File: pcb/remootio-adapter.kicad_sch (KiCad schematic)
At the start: 63 parts, among them J1 AUX, J2 BATT, J3 ICSP, J4 Console, J5 SwitchIn, J6 SPM Connector, U1 remootio-3, U2 LM2940S-5.0, U3 AQV252GAX, U4 ATmega328PB-ANR, U5 ST232CDR, U6 AQV252GAX, U7 AQV252GAX, U8 AQV252GAX, Y1 CSTCE16M0V53-R0

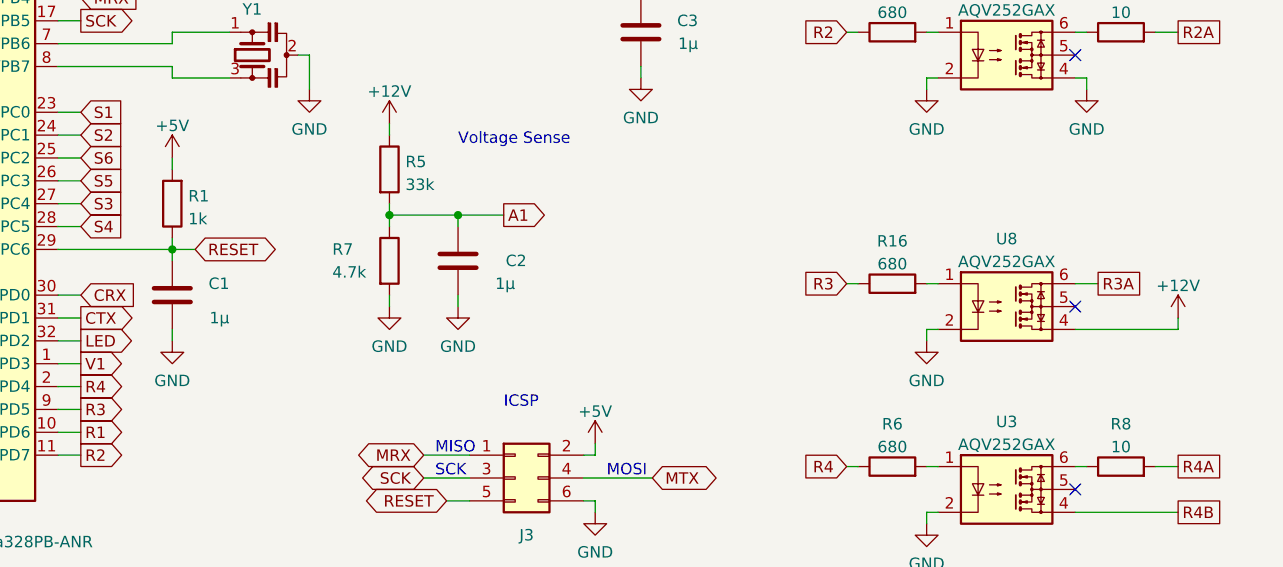
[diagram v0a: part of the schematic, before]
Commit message: Revise PCB layout for production board v1.1
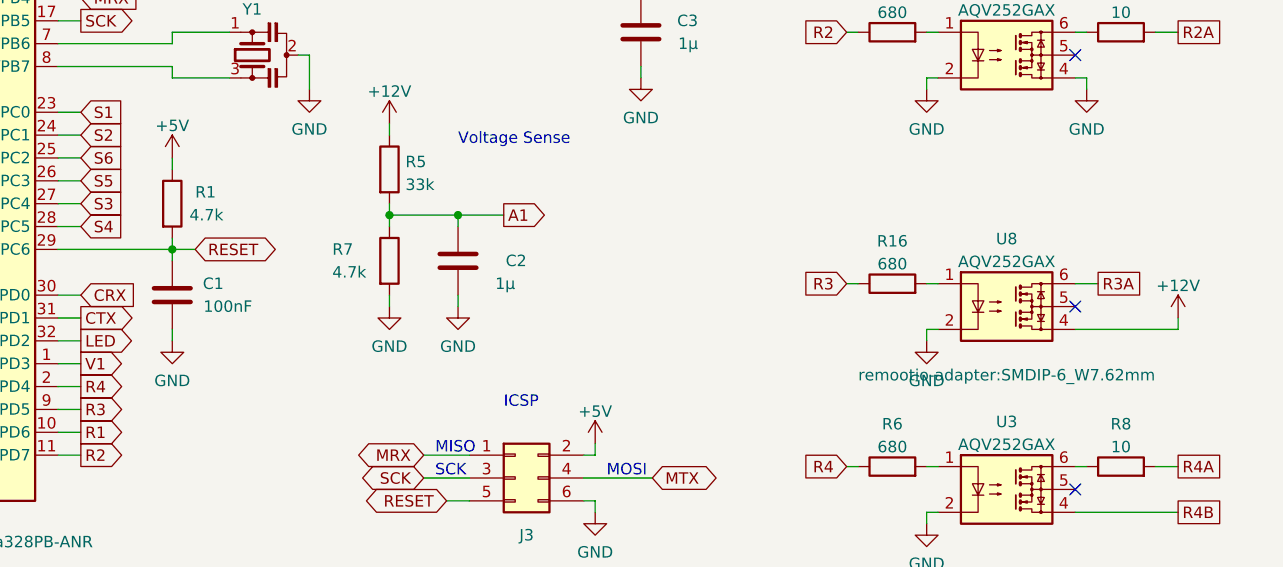
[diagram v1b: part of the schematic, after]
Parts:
- C1: value 1µ -> 100nF; LCSC C86020 -> C14663; PARTNO GRM188R71E105KA12D -> CC0603KRX7R9BB104
- R1: value 1k -> 4.7k; LCSC C21190 -> C23162; PARTNO 0603WAF1001T5E -> 0603WAF4701T5E
- U3, U6, U7, U8: footprint Package_DIP:SMDIP-6_W7.62mm -> remootio-adapter:SMDIP-6_W7.62mm
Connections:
- net +5V: now also R1.1; no longer R1.2
- net RESET: now also R1.2; no longer R1.1
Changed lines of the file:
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@@
   (title_block
     (title "Remootio Adapter - Hay Hoist")
-    (date "2024-07-22")
-    (rev "1.0")
+    (date "2024-07-30")
+    (rev "1.1")
     (company "Hyspec / 6-v")
-    (comment 1 "Ordered 5 @ JLCPCB")
   )
   (junction (at 260.35 33.02) (diameter 0) (color 0 0 0 0)
@@
   (symbol (lib_id "Device:C") (at 161.29 130.81 180) (unit 1)
     (in_bom yes) (on_board yes)
-    (property "Reference" "C1" (id 0) (at 167.64 129.54 0)
+    (property "Reference" "C1" (id 0) (at 167.005 129.54 0)
       (effects (font (size 1.27 1.27)) (justify left))
     )
-    (property "Value" "1µ" (id 1) (at 167.64 133.35 0)
+    (property "Value" "100nF" (id 1) (at 170.18 132.08 0)
       (effects (font (size 1.27 1.27)) (justify left))
     )
@@
       (effects (font (size 1.27 1.27)) hide)
     )
-    (property "Datasheet" "GRM188R71E105KA12D.pdf" (id 3) (at 161.29 130.81 0)
+    (property "Datasheet" "CC0603KRX7R9BB104.pdf" (id 3) (at 161.29 130.81 0)
       (effects (font (size 1.27 1.27)) hide)
     )
-    (property "LCSC" "C86020" (id 4) (at 161.29 130.81 90)
+    (property "LCSC" "C14663" (id 4) (at 161.29 130.81 90)
       (effects (font (size 1.27 1.27)) hide)
     )
-    (property "PARTNO" "GRM188R71E105KA12D" (id 5) (at 161.29 130.81 90)
+    (property "PARTNO" "CC0603KRX7R9BB104" (id 5) (at 161.29 130.81 90)
       (effects (font (size 1.27 1.27)) hide)
     )
@@
     (property "Reference" "U7" (id 0) (at 254 77.5802 0))
     (property "Value" "AQV252GAX" (id 1) (at 254 80.1171 0))
-    (property "Footprint" "Package_DIP:SMDIP-6_W7.62mm" (id 2) (at 254 92.71 0)
+    (property "Footprint" "remootio-adapter:SMDIP-6_W7.62mm" (id 2) (at 254 92.71 0)
       (effects (font (size 1.27 1.27)) hide)
     )
@@
     (pin "1")
   )
-  (symbol (lib_id "Device:R") (at 161.29 120.65 180) (unit 1)
-    (in_bom yes) (on_board yes) (fields_autoplaced)
-    (property "Reference" "R1" (id 0) (at 163.068 119.8153 0)
-      (effects (font (size 1.27 1.27)) (justify right))
-    )
-    (property "Value" "1k" (id 1) (at 163.068 122.3522 0)
-      (effects (font (size 1.27 1.27)) (justify right))
-    )
-    (property "Footprint" "Resistor_SMD:R_0603_1608Metric" (id 2) (at 163.068 120.65 90)
-      (effects (font (size 1.27 1.27)) hide)
-    )
-    (property "Datasheet" "0603WAF1001T5E.pdf" (id 3) (at 161.29 120.65 0)
-      (effects (font (size 1.27 1.27)) hide)
-    )
-    (property "LCSC" "C21190" (id 4) (at 161.29 120.65 90)
-      (effects (font (size 1.27 1.27)) hide)
-    )
-    (property "PARTNO" "0603WAF1001T5E" (id 5) (at 161.29 120.65 90)
-      (effects (font (size 1.27 1.27)) hide)
-    )
-    (pin "1")
-    (pin "2")
-  )
   (symbol (lib_id "Device:C") (at 97.79 144.78 270) (unit 1)
     (in_bom yes) (on_board yes)
@@
     (property "Reference" "U6" (id 0) (at 254 96.6302 0))
     (property "Value" "AQV252GAX" (id 1) (at 254 99.1671 0))
-    (property "Footprint" "Package_DIP:SMDIP-6_W7.62mm" (id 2) (at 254 111.76 0)
+    (property "Footprint" "remootio-adapter:SMDIP-6_W7.62mm" (id 2) (at 254 111.76 0)
       (effects (font (size 1.27 1.27)) hide)
     )
@@
     (pin "2")
   )
+  (symbol (lib_id "Device:R") (at 161.29 120.65 0) (unit 1)
+    (in_bom yes) (on_board yes)
+    (property "Reference" "R1" (id 0) (at 163.83 119.38 0)
+      (effects (font (size 1.27 1.27)) (justify left))
+    )
+    (property "Value" "4.7k" (id 1) (at 163.195 121.92 0)
+      (effects (font (size 1.27 1.27)) (justify left))
+    )
+    (property "Footprint" "Resistor_SMD:R_0603_1608Metric" (id 2) (at 159.512 120.65 90)
+      (effects (font (size 1.27 1.27)) hide)
+    )
+    (property "Datasheet" "0603WAF4701T5E.pdf" (id 3) (at 161.29 120.65 0)
+      (effects (font (size 1.27 1.27)) hide)
+    )
+    (property "LCSC" "C23162" (id 4) (at 161.29 120.65 90)
+      (effects (font (size 1.27 1.27)) hide)
+    )
+    (property "PARTNO" "0603WAF4701T5E" (id 5) (at 161.29 120.65 90)
+      (effects (font (size 1.27 1.27)) hide)
+    )
+    (pin "1")
+    (pin "2")
+  )
   (symbol (lib_id "power:GND") (at 193.04 132.08 0) (unit 1)
     (in_bom yes) (on_board yes) (fields_autoplaced)
@@
     (property "Reference" "U3" (id 0) (at 254 144.8902 0))
     (property "Value" "AQV252GAX" (id 1) (at 254 147.4271 0))
-    (property "Footprint" "Package_DIP:SMDIP-6_W7.62mm" (id 2) (at 254 160.02 0)
+    (property "Footprint" "remootio-adapter:SMDIP-6_W7.62mm" (id 2) (at 254 160.02 0)
       (effects (font (size 1.27 1.27)) hide)
     )
@@
     (property "Reference" "U8" (id 0) (at 254 124.5702 0))
     (property "Value" "AQV252GAX" (id 1) (at 254 127.1071 0))
-    (property "Footprint" "Package_DIP:SMDIP-6_W7.62mm" (id 2) (at 254 139.7 0)
-      (effects (font (size 1.27 1.27)) hide)
-    )
+    (property "Footprint" "remootio-adapter:SMDIP-6_W7.62mm" (id 2) (at 254 139.7 0))
     (property "Datasheet" "AQV252GAX.pdf" (id 3) (at 254 132.08 0)
       (effects (font (size 0 0)) hide)
@@
     )
     (path "/60b60661-5441-4720-a9c2-d24e0064a5a0"
-      (reference "C1") (unit 1) (value "1µ") (footprint "Capacitor_SMD:C_0603_1608Metric")
+      (reference "C1") (unit 1) (value "100nF") (footprint "Capacitor_SMD:C_0603_1608Metric")
     )
     (path "/7e705115-9ba3-4ade-9c21-0ecd8cb7d552"
@@
       (reference "J6") (unit 1) (value "SPM Connector") (footprint "TerminalBlock_Phoenix:TerminalBlock_Phoenix_MKDS-1,5-8-5.08_1x08_P5.08mm_Horizontal")
     )
-    (path "/8234446a-2afe-4a9b-9a53-39dd33467d7e"
-      (reference "R1") (unit 1) (value "1k") (footprint "Resistor_SMD:R_0603_1608Metric")
+    (path "/b6fb716c-d73d-4cb2-82ba-361713ac886b"
+      (reference "R1") (unit 1) (value "4.7k") (footprint "Resistor_SMD:R_0603_1608Metric")
     )
     (path "/5de2599c-fbeb-484b-8fcf-91d79ad8d43b"
@@
     )
     (path "/c1bc3891-d4c5-4a3d-af07-e42d28535bf4"
-      (reference "U3") (unit 1) (value "AQV252GAX") (footprint "Package_DIP:SMDIP-6_W7.62mm")
+      (reference "U3") (unit 1) (value "AQV252GAX") (footprint "remootio-adapter:SMDIP-6_W7.62mm")
     )
     (path "/ebaf2b81-8432-4142-9920-6faf4f23aa7d"
@@
     )
     (path "/a85d6911-9680-422b-a8e9-1367fbf4022a"
-      (reference "U6") (unit 1) (value "AQV252GAX") (footprint "Package_DIP:SMDIP-6_W7.62mm")
+      (reference "U6") (unit 1) (value "AQV252GAX") (footprint "remootio-adapter:SMDIP-6_W7.62mm")
     )
     (path "/7bad97ee-b0f3-485e-b963-4bac43e534c7"
-      (reference "U7") (unit 1) (value "AQV252GAX") (footprint "Package_DIP:SMDIP-6_W7.62mm")
+      (reference "U7") (unit 1) (value "AQV252GAX") (footprint "remootio-adapter:SMDIP-6_W7.62mm")
     )
     (path "/d3bed3fa-52c1-4a23-9ef9-5c53ebed779a"
-      (reference "U8") (unit 1) (value "AQV252GAX") (footprint "Package_DIP:SMDIP-6_W7.62mm")
+      (reference "U8") (unit 1) (value "AQV252GAX") (footprint "remootio-adapter:SMDIP-6_W7.62mm")
     )
     (path "/4c0707aa-6e6f-4ade-ba13-26f73eef7bfd"

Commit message: Minor cosmetic footprint adjustment
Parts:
- D1: footprint LED_THT:LED_D3.0mm_Clear -> remootio-adapter:bivar-led
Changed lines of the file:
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@@
   (title_block
     (title "Remootio Adapter - Hay Hoist")
-    (date "2024-07-30")
+    (date "2024-08-06")
     (rev "1.1")
     (company "Hyspec / 6-v")
@@
     (property "Reference" "D1" (id 0) (at 217.4875 71.6112 0))
     (property "Value" "VAOL-3GWY4" (id 1) (at 217.4875 74.1481 0))
-    (property "Footprint" "LED_THT:LED_D3.0mm_Clear" (id 2) (at 215.9 77.47 0)
+    (property "Footprint" "remootio-adapter:bivar-led" (id 2) (at 215.9 77.47 0)
       (effects (font (size 1.27 1.27)) hide)
     )
@@
     )
     (path "/edcf1849-349d-4d22-9ff8-a3b3b9d08838"
-      (reference "D1") (unit 1) (value "VAOL-3GWY4") (footprint "LED_THT:LED_D3.0mm_Clear")
+      (reference "D1") (unit 1) (value "VAOL-3GWY4") (footprint "remootio-adapter:bivar-led")
     )
     (path "/201afaf1-c2db-44e9-a493-4de777d50aa5"

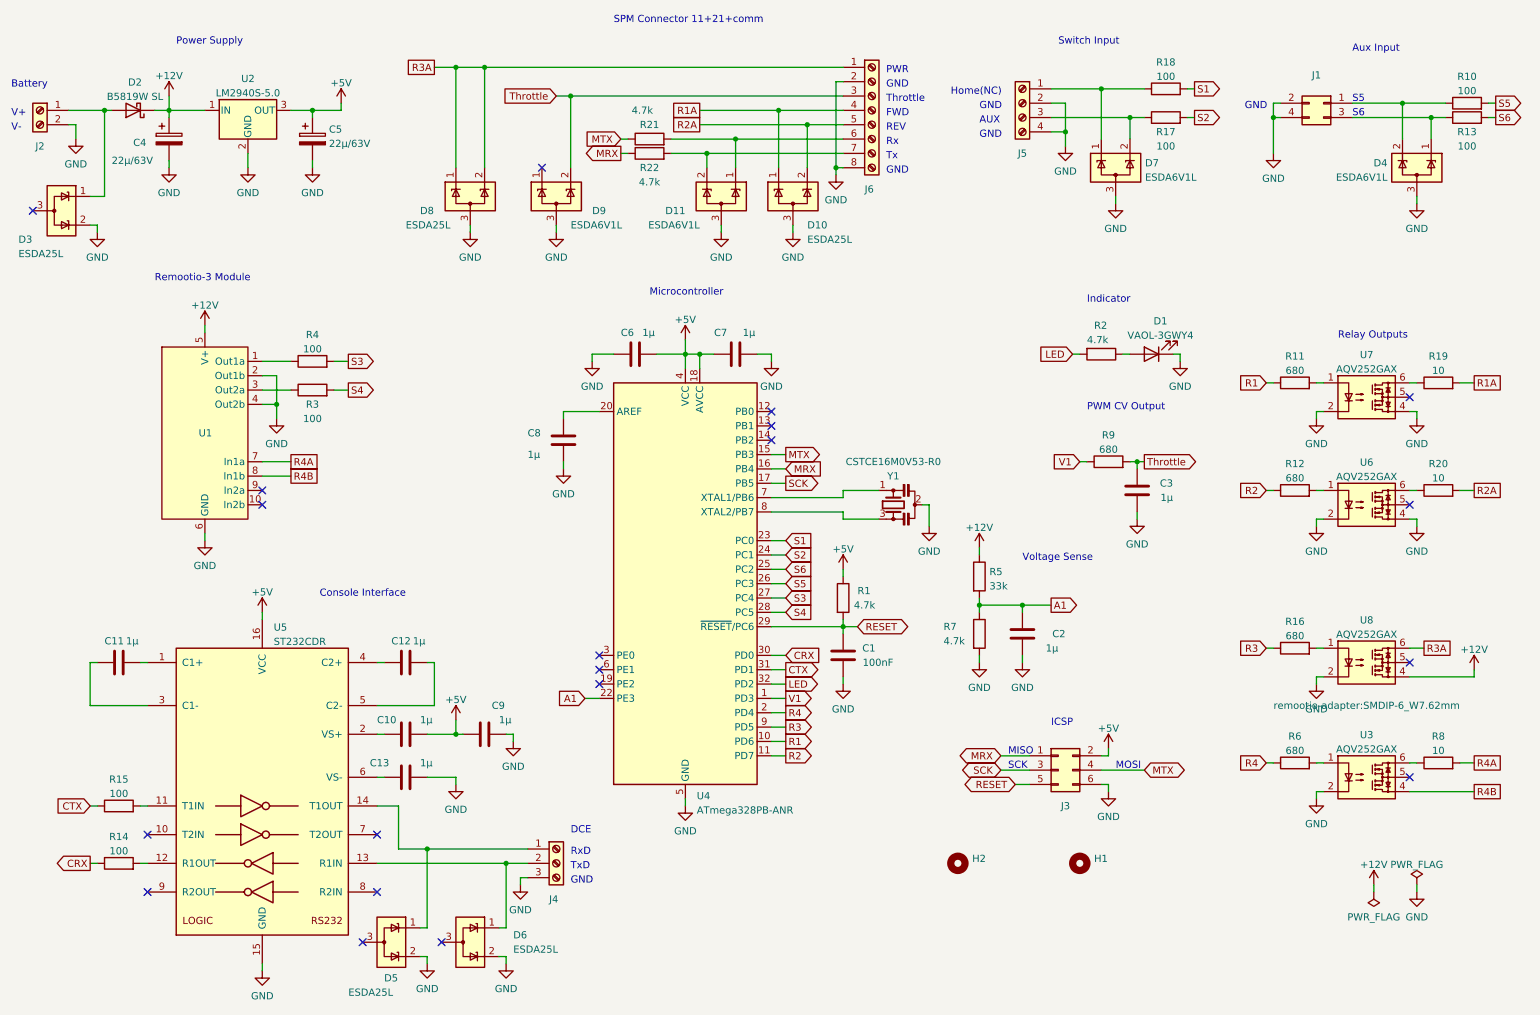
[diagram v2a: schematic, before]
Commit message: Jostle footprints onto 0.5mm grid and change terminals to 5mm pitch
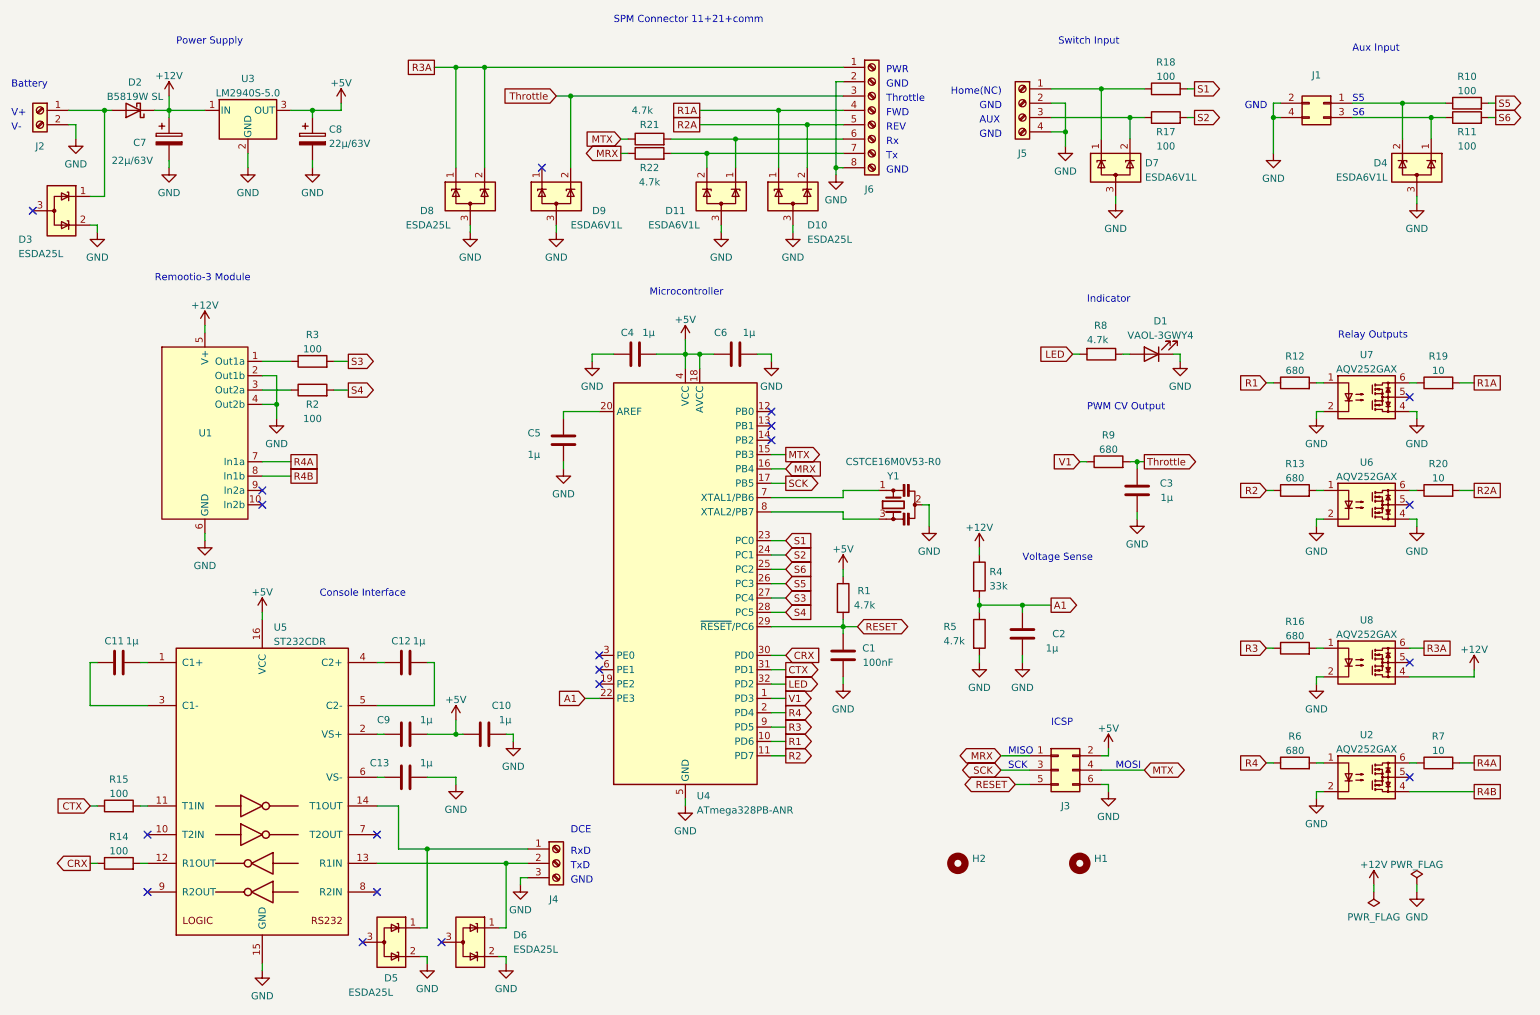
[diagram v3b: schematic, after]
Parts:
- J2: footprint TerminalBlock_Phoenix:TerminalBlock_Phoenix_MKDS-1,5-2-5.08_1x02_P5.08mm_Horizontal -> TerminalBlock_Phoenix:TerminalBlock_Phoenix_PT-1,5-2-5.0-H_1x02_P5.00mm_Horizontal
- J4: footprint TerminalBlock_Phoenix:TerminalBlock_Phoenix_MKDS-1,5-3-5.08_1x03_P5.08mm_Horizontal -> TerminalBlock_Phoenix:TerminalBlock_Phoenix_PT-1,5-3-5.0-H_1x03_P5.00mm_Horizontal
- J5: footprint TerminalBlock_Phoenix:TerminalBlock_Phoenix_MKDS-1,5-4-5.08_1x04_P5.08mm_Horizontal -> TerminalBlock_Phoenix:TerminalBlock_Phoenix_PT-1,5-4-5.0-H_1x04_P5.00mm_Horizontal
- J6: footprint TerminalBlock_Phoenix:TerminalBlock_Phoenix_MKDS-1,5-8-5.08_1x08_P5.08mm_Horizontal -> TerminalBlock_Phoenix:TerminalBlock_Phoenix_PT-1,5-8-5.0-H_1x08_P5.00mm_Horizontal
- renumbered C9 to C10, C6 to C4, C8 to C5, C7 to C6, C4 to C7, C5 to C8, C10 to C9, R13 to R11, R11 to R12, R12 to R13, R3 to R2, R4 to R3, R5 to R4, R7 to R5, R8 to R7, R2 to R8, U3 to U2, U2 to U3
